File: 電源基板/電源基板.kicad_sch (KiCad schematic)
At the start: 19 parts, among them J1 XT30, J2 PWR out, J3 Power Switch, J4 5V out, Q2 Q_NMOS_GDS, U1 OKL-T/6-W12N-C

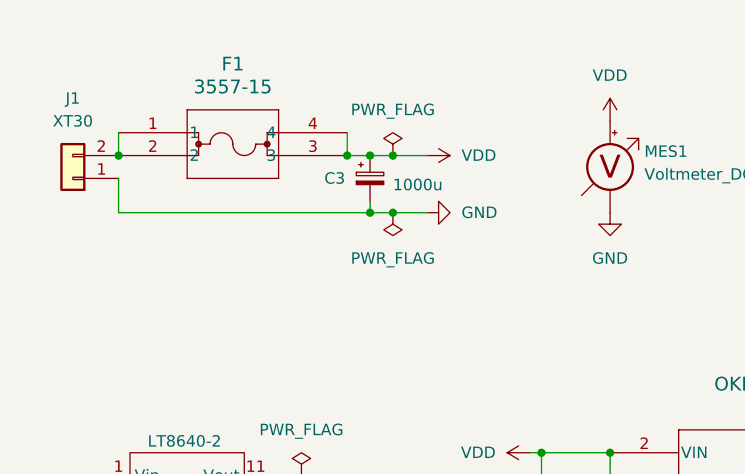
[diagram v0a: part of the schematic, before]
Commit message: パスコンと保護ダイオードの追加
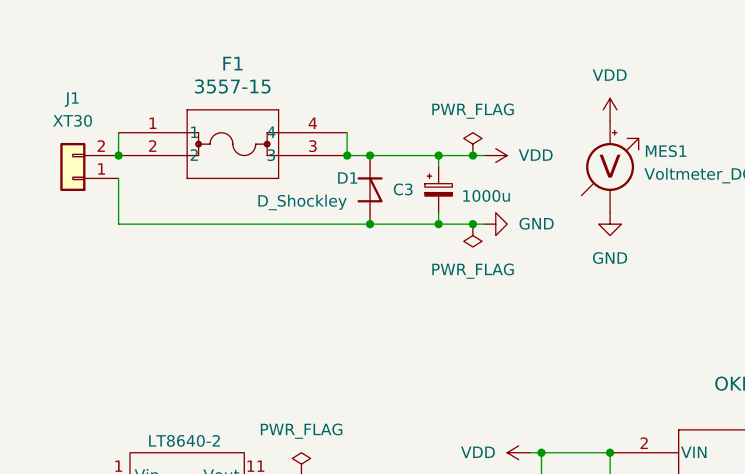
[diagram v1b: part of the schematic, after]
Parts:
- added D1: D_Shockley, Diode_THT:D_DO-201AD_P12.70mm_Horizontal, symbol Device:D_Shockley
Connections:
- net GND: now also D1.2 (A)
- net VDD: now also D1.1 (K)
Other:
- moved on the sheet: C3

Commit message: サーボ基板
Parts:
- added J5: Conn_01x02_Pin, Connector_PinHeader_2.54mm:PinHeader_1x02_P2.54mm_Vertical, symbol Connector:Conn_01x02_Pin
- renumbered LT8640-2 to LT8640-1
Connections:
- net GND2: now also J5.1 (Pin_1)
- net VDD: now also J5.2 (Pin_2)

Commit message: 電源基板
白色にして発注
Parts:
- removed C1: 22u, Capacitor_SMD:C_0603_1608Metric_Pad1.08x0.95mm_HandSolder, symbol Device:C_Small
- removed C2: 10u, Capacitor_SMD:C_0603_1608Metric_Pad1.08x0.95mm_HandSolder, symbol Device:C_Small
- removed J2: PWR out, Connector_AMASS:AMASS_XT30U-F_1x02_P5.0mm_Vertical, symbol Connector_Generic:Conn_01x02
- removed J4: 5V out, Connector_JST:JST_VH_B3P-VH_1x03_P3.96mm_Vertical, symbol Connector_Generic:Conn_01x03
- removed JP1: JumperShort, Connector_PinHeader_2.54mm:PinHeader_1x02_P2.54mm_Vertical, symbol Jumper:Jumper_2_Open
- removed R4: R_Small, Resistor_SMD:R_0603_1608Metric_Pad0.98x0.95mm_HandSolder, symbol Device:R_Small
- removed RV2: 20k, Potentiometer_THT:Potentiometer_Bourns_3296W_Vertical, symbol Device:R_Potentiometer_Small
- removed U1: OKL-T/6-W12N-C, OKL-T_6-W12N-C:DCDC-murata-6A, symbol 2024-09-15_15-34-43:OKL-T_6-W12N-C
- added D3: RED, LED_THT:LED_D5.0mm_Horizontal_O3.81mm_Z3.0mm, symbol Device:LED_Small
- added J2: Conn_01x02_Pin, Connector_PinHeader_2.54mm:PinHeader_1x02_P2.54mm_Vertical, symbol Connector:Conn_01x02_Pin
- added J4: PWR OUT, Connector_JST:JST_VH_B5P-VH_1x05_P3.96mm_Vertical, symbol Connector_Generic:Conn_01x05
- added LT8640-2, LT8640-3: ~, LT8640:LT8640, symbol LT8640:LT8640
- added U1: ATtiny85-20P, Package_DIP:DIP-8_W7.62mm, symbol MCU_Microchip_ATtiny:ATtiny85-20P
- R1: value 20k -> 220
- R2, R3: value 1.2k -> R_Small
- renumbered J5 to FAN1
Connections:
- net +5VD is gone; now on net VDD: R2.1
- net GND2: now also LT8640-2.10 (GND), LT8640-2.8 (GND), LT8640-2.9 (GND), LT8640-3.10 (GND), LT8640-3.8 (GND), LT8640-3.9 (GND); no longer LT8640-1.14 (GND), LT8640-1.15 (GND), LT8640-1.16 (GND), R2.2, R3.2
- net VDD: now also LT8640-2.1 (Vin), LT8640-2.2 (Vin), LT8640-2.3 (Vin), LT8640-3.1 (Vin), LT8640-3.2 (Vin), LT8640-3.3 (Vin); no longer R1.1
- net init_6v: now reaches LT8640-1.4 (EN/UV)
- net init_6v: now also LT8640-2.4 (EN/UV), U1.5 (AREF/PB0)
- net GND3: now reaches R1.2
- net GND3: now also R3.2, J2.1 (Pin_1), J4.1 (Pin_1), LT8640-3.14 (GND), LT8640-3.15 (GND), LT8640-3.16 (GND), U1.4 (GND)
- net Vref: now reaches R3.1
- net Vref: now also R2.2, U1.7 (PB2)
- net +5VA renamed 6VA
- net 6VA: now also J4.5 (Pin_5)
- new net: D3.1 (K), R1.1
- new net +5V: J4.2 (Pin_2), LT8640-3.11 (Vout), LT8640-3.12 (Vout), LT8640-3.13 (Vout), U1.8 (VCC)
- new net 6VB: J4.4 (Pin_4), LT8640-2.11 (Vout), LT8640-2.12 (Vout), LT8640-2.13 (Vout)
- new net GND1: J4.3 (Pin_3), LT8640-1.14 (GND), LT8640-1.15 (GND), LT8640-1.16 (GND), LT8640-2.14 (GND), LT8640-2.15 (GND), LT8640-2.16 (GND)
- new net init_5v: LT8640-3.4 (EN/UV), U1.6 (PB1)
- new net led: D3.2 (A), U1.2 (XTAL1/PB3)
- new net tx: J2.2 (Pin_2), U1.3 (XTAL2/PB4)
- no-connect marks 6 -> 10
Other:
- moved on the sheet: FAN1, LT8640-1

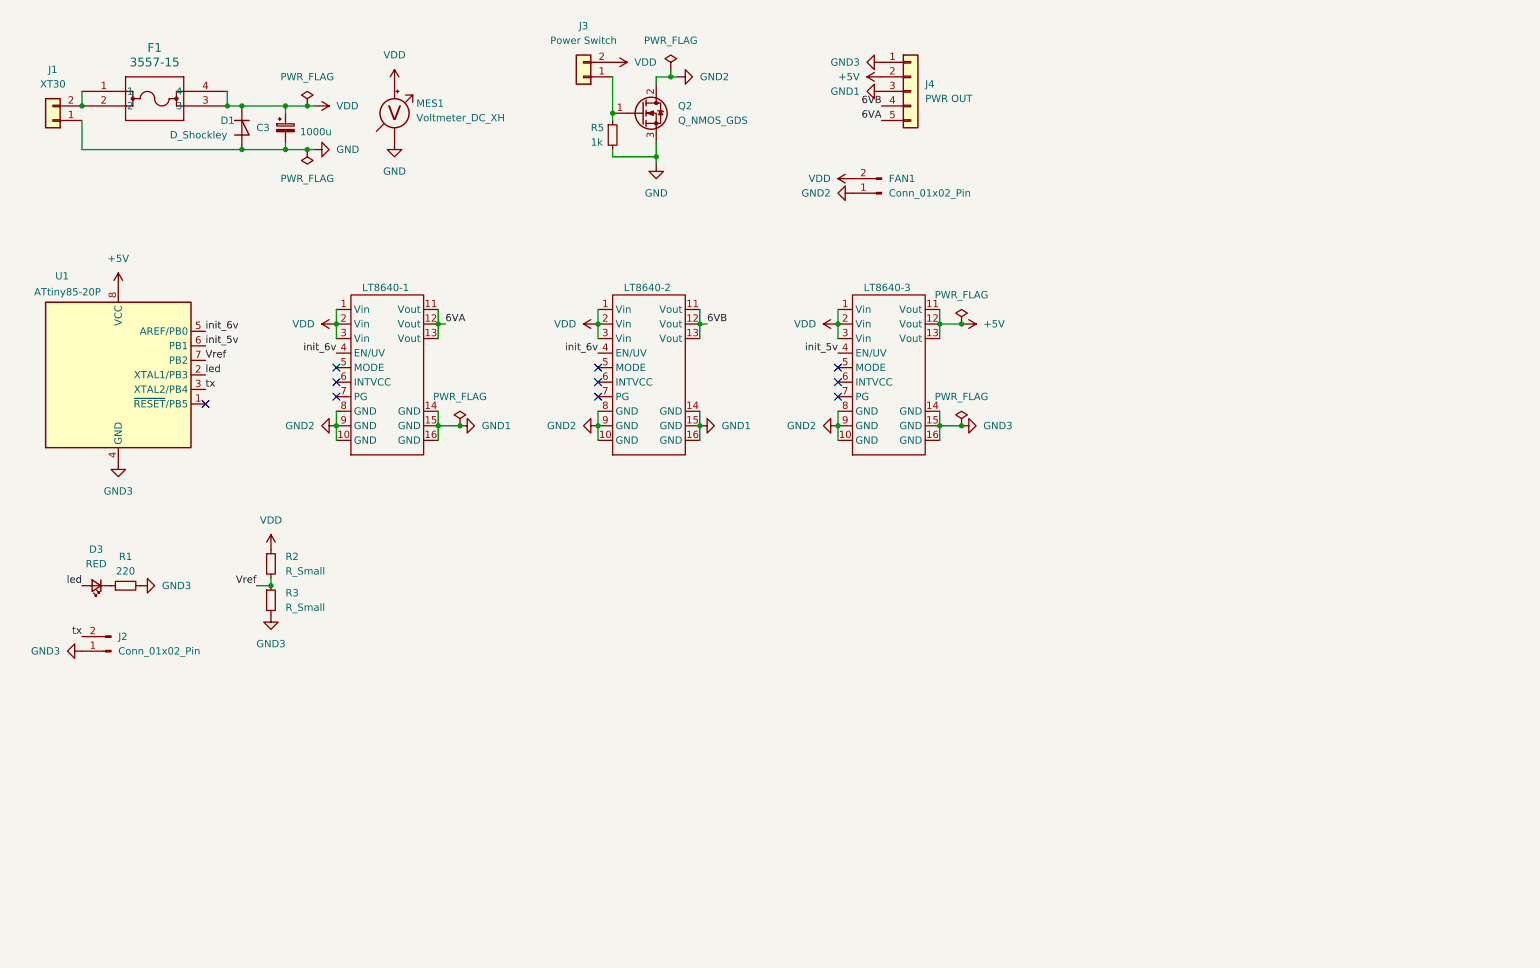
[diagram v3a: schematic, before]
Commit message: 電源基板にATtiny用LDOを追加
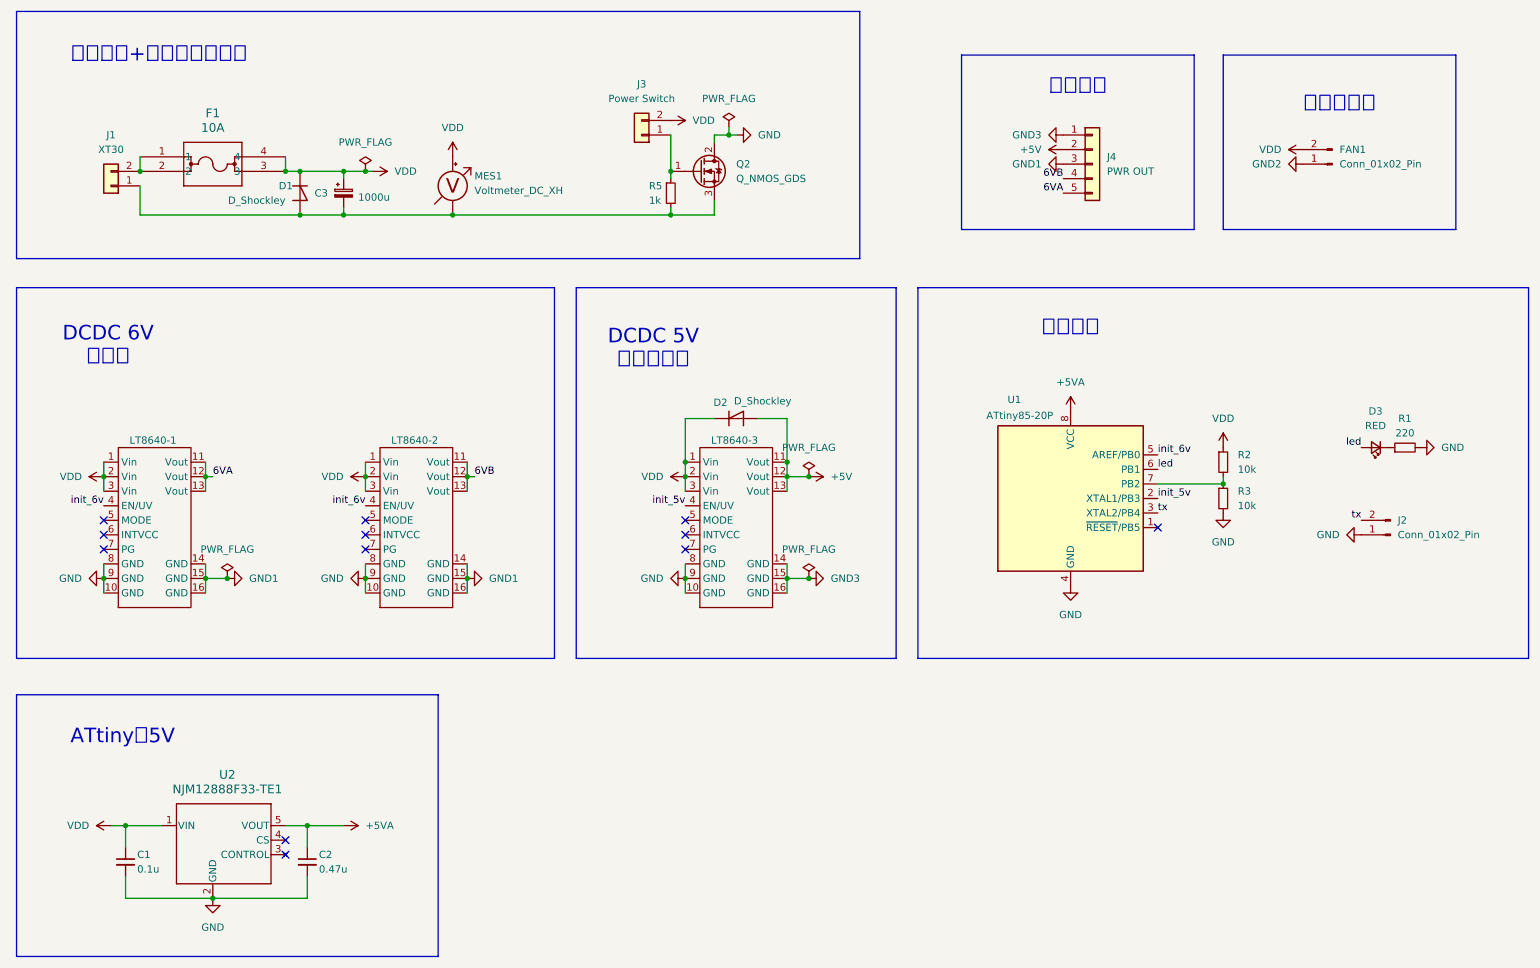
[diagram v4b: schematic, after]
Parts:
- added C1: 0.1u, Capacitor_SMD:C_0603_1608Metric_Pad1.08x0.95mm_HandSolder, symbol Device:C_Small
- added C2: 0.47u, Capacitor_SMD:C_0603_1608Metric_Pad1.08x0.95mm_HandSolder, symbol Device:C_Small
- added D2: D_Shockley, Diode_THT:D_DO-201AD_P12.70mm_Horizontal, symbol Device:D_Shockley
- added U2: NJM12888F33-TE1, PI-SOT-23-5-E-A_NMD, symbol NJM12888:NJM12888F33-TE1
- F1: value 3557-15 -> 10A
- R2, R3: value R_Small -> 10k
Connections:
- net +5V: now also D2.2 (A); no longer U1.8 (VCC)
- net GND: now also J2.1 (Pin_1), LT8640-1.10 (GND), LT8640-1.8 (GND), LT8640-1.9 (GND), LT8640-2.10 (GND), LT8640-2.8 (GND), LT8640-2.9 (GND), LT8640-3.10 (GND), LT8640-3.8 (GND), LT8640-3.9 (GND), Q2.2 (D), R1.2, R3.2, U1.4 (GND), C1.2, C2.2, U2.2 (GND); no longer C3.2, D1.2 (A), J1.1 (Pin_1), MES1.1 (-), Q2.3 (S), R5.2
- net GND2: no longer LT8640-1.10 (GND), LT8640-1.8 (GND), LT8640-1.9 (GND), LT8640-2.10 (GND), LT8640-2.8 (GND), LT8640-2.9 (GND), LT8640-3.10 (GND), LT8640-3.8 (GND), LT8640-3.9 (GND), Q2.2 (D)
- net GND3: no longer J2.1 (Pin_1), R1.2, R3.2, U1.4 (GND)
- net VDD: now also C1.1, D2.1 (K), U2.1 (VIN)
- net init_5v: now also U1.2 (XTAL1/PB3); no longer U1.6 (PB1)
- net led: now also U1.6 (PB1); no longer U1.2 (XTAL1/PB3)
- net Vref: no longer names the net of R2.2, R3.1, U1.7 (PB2)
- new net: C3.2, D1.2 (A), J1.1 (Pin_1), MES1.1 (-), Q2.3 (S), R5.2
- new net +5VA: C2.1, U1.8 (VCC), U2.5 (VOUT)
- no-connect marks 10 -> 12
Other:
- note added: "ATtiny用5V"
- note added: "DCDC 5V ロジック系"
- note added: "DCDC 6V 駆動系"
- note added: "冷却ファン"
- note added: "外部出力"
- note added: "電圧管理"
- note added: "電源入力+ロードスイッチ"
- moved on the sheet: C3, D1, D3, F1, FAN1, J1, J2, J3, J4, LT8640-1, LT8640-2, LT8640-3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
